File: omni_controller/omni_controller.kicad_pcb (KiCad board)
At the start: 2 copper layers, 14 parts, among them Q1 2SC1815, U1 XH_4, U2 XH_4, U3 XH_4, U4 XH_4, U5 LPC1768, U6 MPU6050, U7 R3008SB, U8 MCP2561-E-P, U9 XH_2

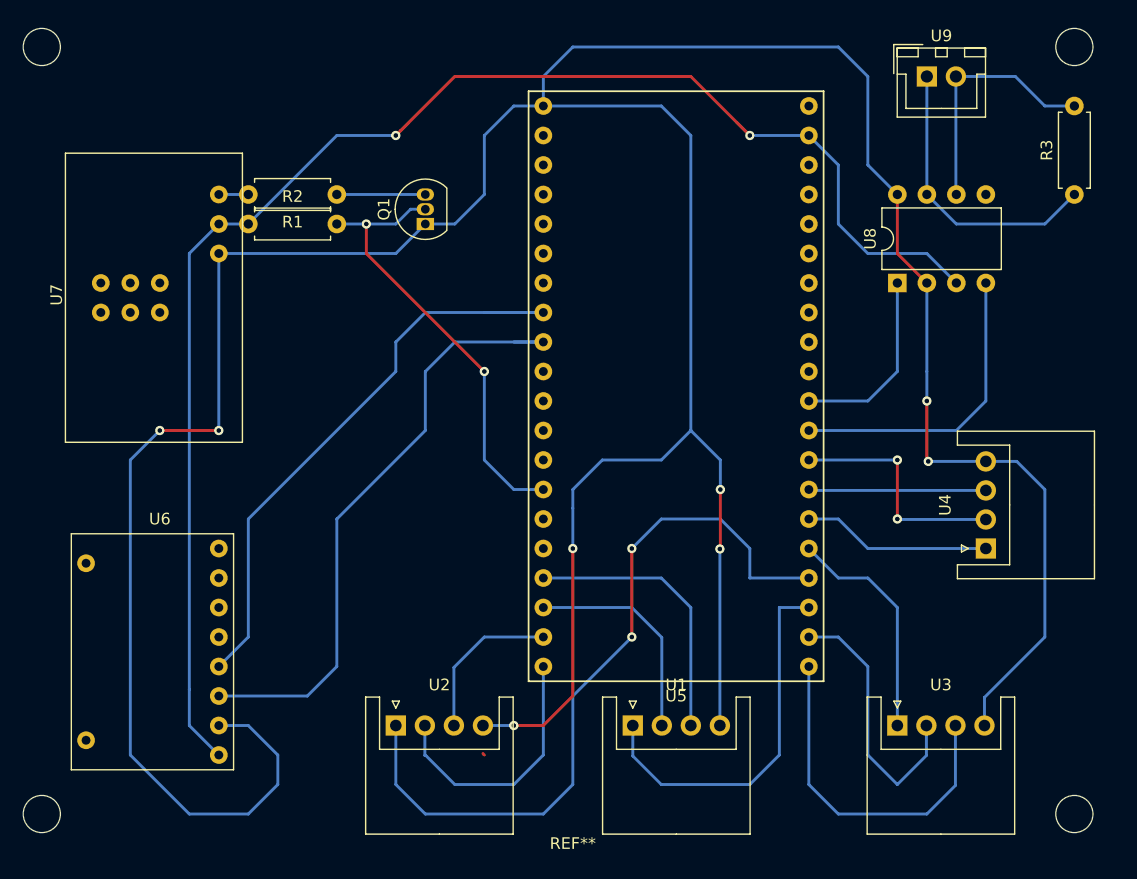
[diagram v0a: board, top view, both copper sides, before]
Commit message: update: ライブラリの更新
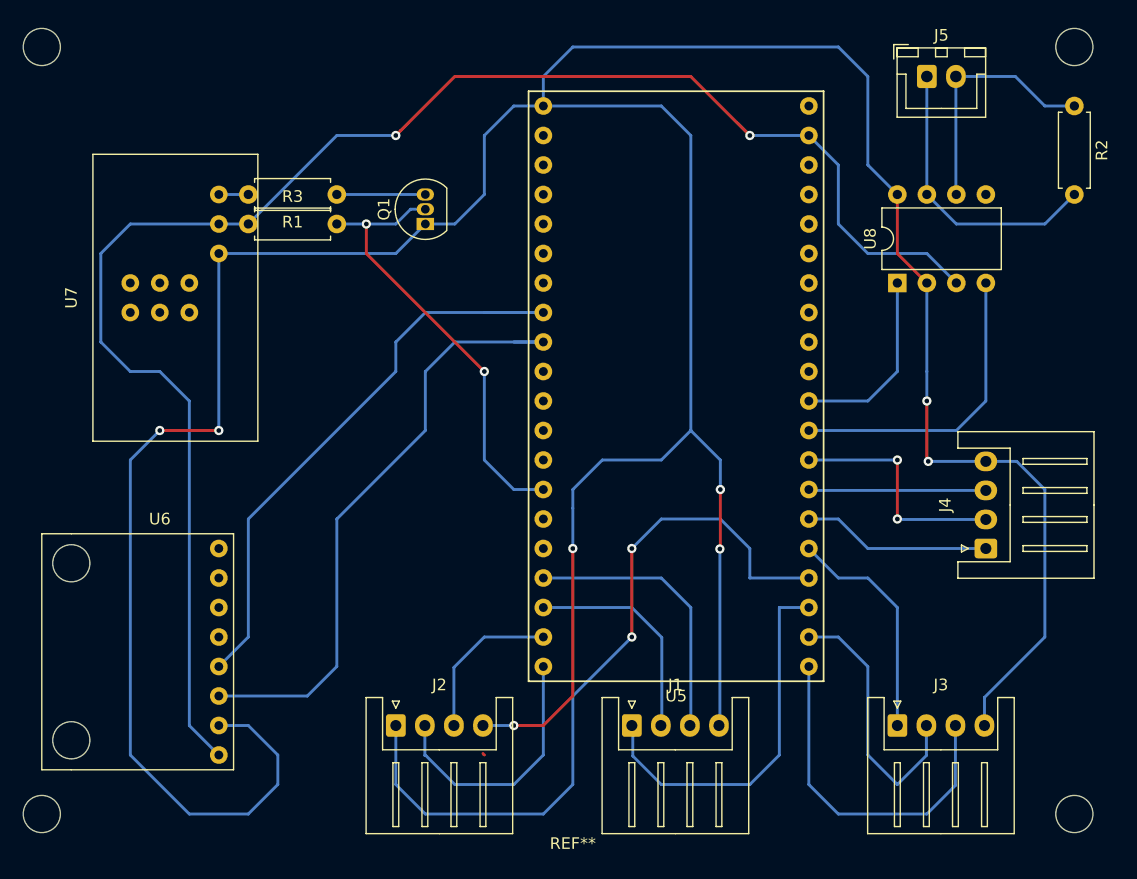
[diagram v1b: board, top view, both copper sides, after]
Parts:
- removed U1, U2, U3, U4: XH_4, MyFootprint:JST_XH_S04B-XH-A_04x2.50mm_Angled
- removed U9: XH_2, MyFootprint:JST_XH_B02B-XH-A_02x2.50mm_Straight
- added J1: Conn_01x04_Male, Connector_JST:JST_XH_S4B-XH-A_1x04_P2.50mm_Horizontal, F.Cu at (149.9, 124.5)
- added J2: Conn_01x04_Male, Connector_JST:JST_XH_S4B-XH-A_1x04_P2.50mm_Horizontal, F.Cu at (129.5, 124.5)
- added J3: Conn_01x04_Male, Connector_JST:JST_XH_S4B-XH-A_1x04_P2.50mm_Horizontal, F.Cu at (172.7, 124.5)
- added J4: Conn_01x04_Male, Connector_JST:JST_XH_S4B-XH-A_1x04_P2.50mm_Horizontal, F.Cu at (180.3, 109.2)
- added J5: Conn_01x02_Male, Connector_JST:JST_XH_B2B-XH-A_1x02_P2.50mm_Vertical, F.Cu at (175.3, 68.6)
- moved R2 71.8 mm to (188.0, 71.1), turned to 270 degrees
- moved R3 71.2 mm to (116.8, 81.3), turned to 0 degrees
- moved U7 3.57 mm to (111.8, 87.6)
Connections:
- R2 pad 1: +5V -> CAN_L
- R2 pad 2: Serial_rx -> CAN_H
- R3 pad 1: CAN_H -> +5V
- R3 pad 2: CAN_L -> Serial_rx
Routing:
- net +5V: track 130.0 -> 142.3 mm
